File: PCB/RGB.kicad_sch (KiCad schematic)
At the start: 75 parts, among them J9 RGB_EX

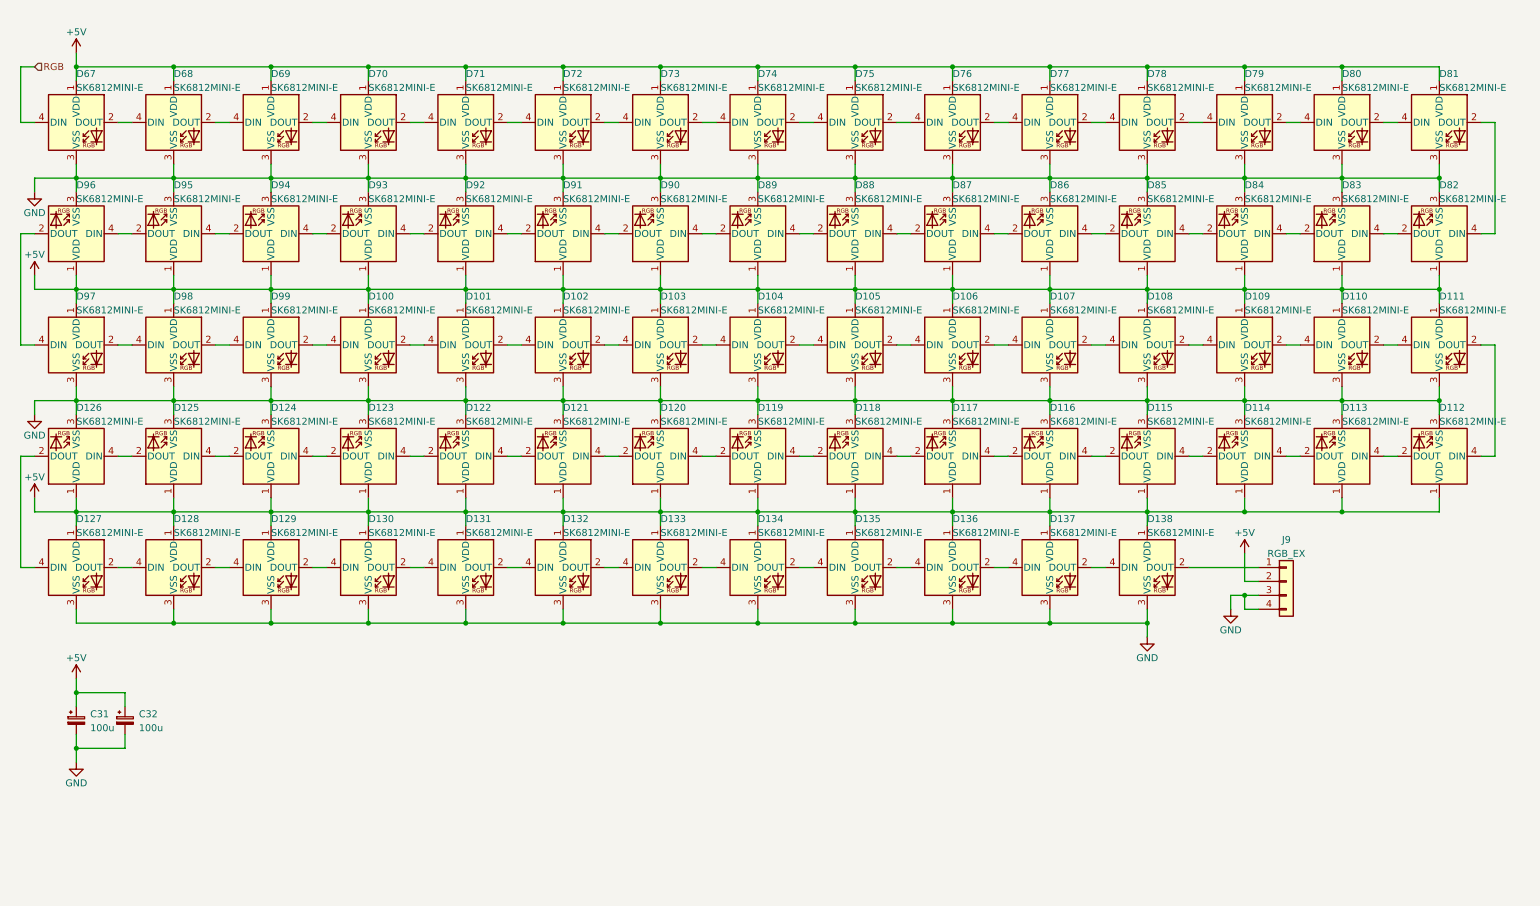
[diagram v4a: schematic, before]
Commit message: 3/4-done update.
Added current and voltage measurement for VBUS in and current measurement for the RGB output. Added PMOS power switch to fully turn off RGB LEDs when not in use. Rerouted the PCB. Moved OLED ribbon cable cutout and expanded it length-wise. Changed position of various components for better routing. Changed bulk capacitance of RGB LEDs to 5 x 22u capacitors. Changed the four N mosfets to two much smaller dual N mosfets. Still need to do RGB routing!
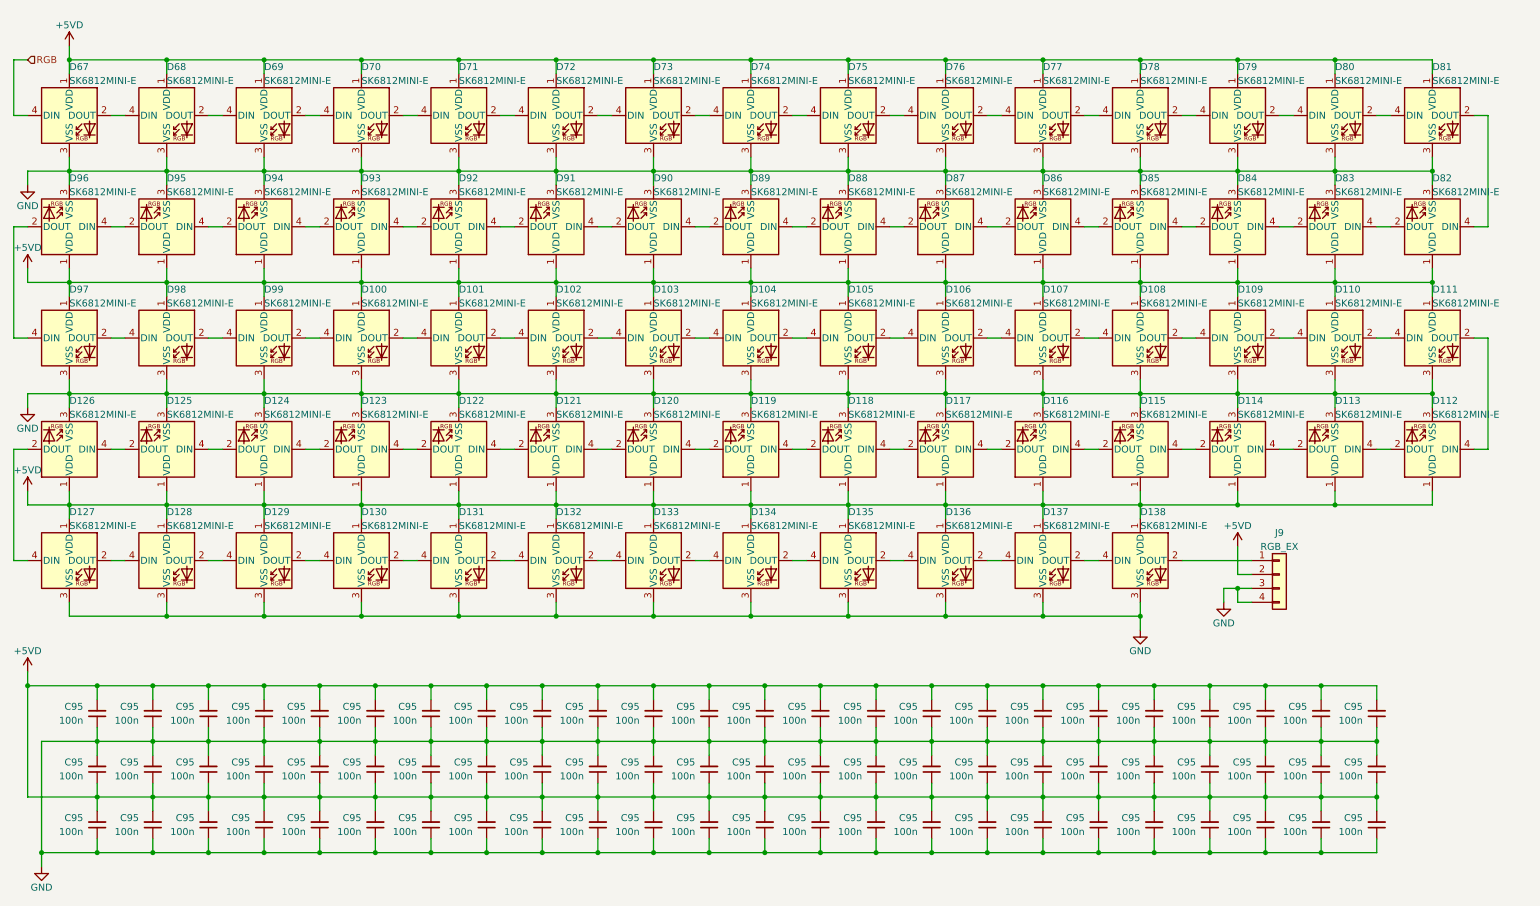
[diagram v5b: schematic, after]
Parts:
- removed C31, C32: 100u, Capacitor_Tantalum_SMD:CP_EIA-6032-15_Kemet-U, symbol Device:C_Polarized_Small
- added C95 (x72): 100n, Capacitor_SMD:C_0402_1005Metric, symbol Device:C_Small
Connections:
- net GND: now also C95.1, C95.1, C95.1, C95.1, C95.1, C95.1, C95.1, C95.1, C95.1, C95.1, C95.1, C95.1, C95.1, C95.1, C95.1, C95.1, C95.1, C95.1, C95.1, C95.1, C95.1, C95.1, C95.1, C95.1, C95.1, C95.1, C95.1, C95.1, C95.1, C95.1, C95.1, C95.1, C95.1, C95.1, C95.1, C95.1, C95.1, C95.1, C95.1, C95.1, C95.1, C95.1, C95.1, C95.1, C95.1, C95.1, C95.1, C95.1, C95.2, C95.2, C95.2, C95.2, C95.2, C95.2, C95.2, C95.2, C95.2, C95.2, C95.2, C95.2, C95.2, C95.2, C95.2, C95.2, C95.2, C95.2, C95.2, C95.2, C95.2, C95.2, C95.2, C95.2
- net +5V renamed +5VD
- net +5VD: now also C95.1, C95.1, C95.1, C95.1, C95.1, C95.1, C95.1, C95.1, C95.1, C95.1, C95.1, C95.1, C95.1, C95.1, C95.1, C95.1, C95.1, C95.1, C95.1, C95.1, C95.1, C95.1, C95.1, C95.1, C95.2, C95.2, C95.2, C95.2, C95.2, C95.2, C95.2, C95.2, C95.2, C95.2, C95.2, C95.2, C95.2, C95.2, C95.2, C95.2, C95.2, C95.2, C95.2, C95.2, C95.2, C95.2, C95.2, C95.2, C95.2, C95.2, C95.2, C95.2, C95.2, C95.2, C95.2, C95.2, C95.2, C95.2, C95.2, C95.2, C95.2, C95.2, C95.2, C95.2, C95.2, C95.2, C95.2, C95.2, C95.2, C95.2, C95.2, C95.2
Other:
- moved on the sheet: D100, D101, D102, D103, D104, D105, D106, D107, D108, D109, D110, D111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
